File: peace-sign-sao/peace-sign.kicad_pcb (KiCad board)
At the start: 2 copper layers, 82.1 x 82.1 mm, 19 parts, among them X1 Badgelife_sao_connector_v169b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

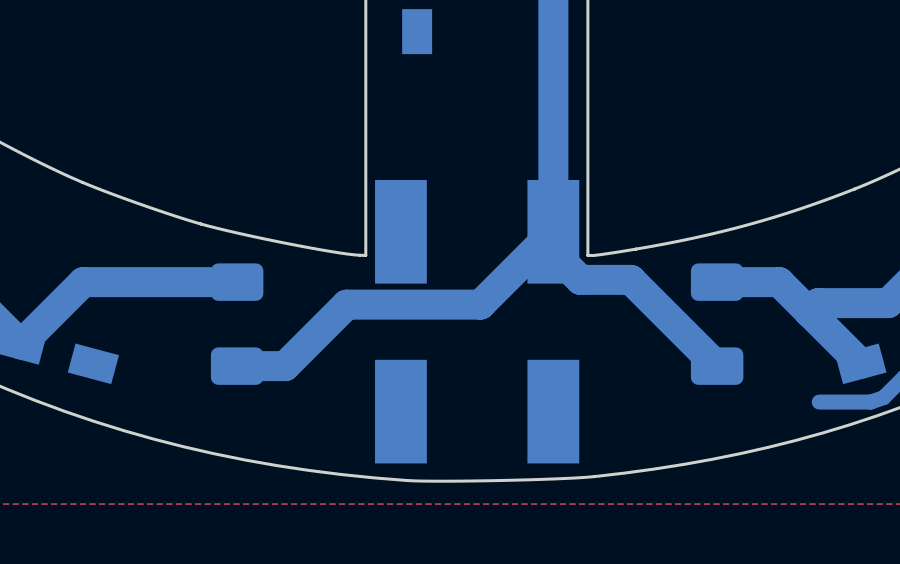
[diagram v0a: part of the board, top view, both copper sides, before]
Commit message: peace-sign-sao: change SAO connector back to 6 pin for stability
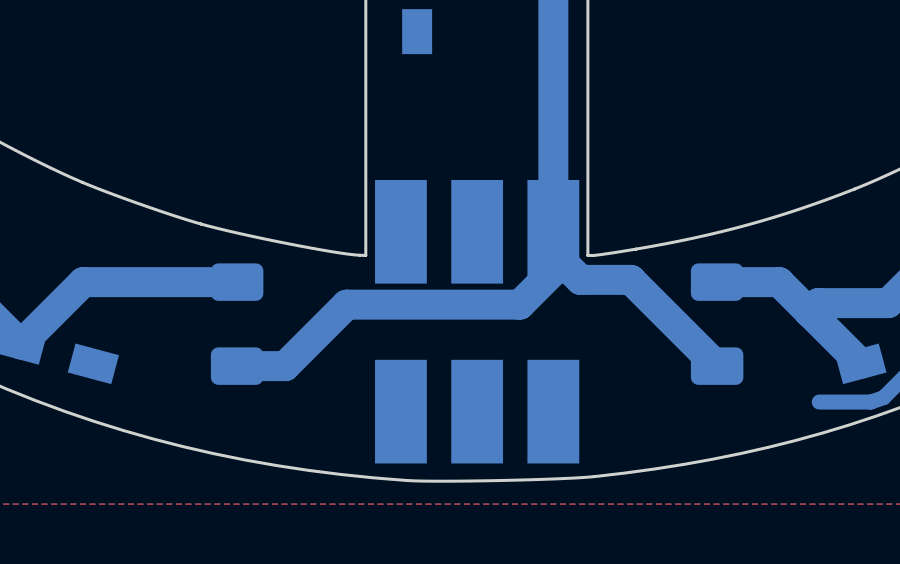
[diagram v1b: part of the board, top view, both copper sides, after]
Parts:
- X1: footprint tom-connectors:Badgelife-SAOv169-SAO-2x3-SMD-NOCENTREPINS -> tom-connectors:Badgelife-SAOv169-SAO-2x3-SMD
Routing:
- net +3V3: track 53.0 -> 53.8 mm

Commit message: peace-sign-sao: as submitted
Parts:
- moved R2 0.91 mm to (107.9, 93.9), turned to 0 degrees
- moved R3 0.50 mm to (91.7, 93.4), turned to 180 degrees
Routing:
- net /ANODE3: track 58.1 -> 54.5 mm
- net GND: track 4.63 -> 7.50 mm
- net /ANODE2: track 97.1 -> 94.9 mm
- net /ANODE1: track 97.0 -> 99.2 mm
- net /ANODE4: track 44.7 -> 46.5 mm
- net +3V3: track 53.8 -> 52.2 mm
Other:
- board text added: "JLCJLCJLCJLC"
